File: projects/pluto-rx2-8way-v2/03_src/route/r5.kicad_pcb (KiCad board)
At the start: 4 copper layers, 50 x 73 mm, 32 parts

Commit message: the stranded GND pads were never a search problem: a router reserves a barrel window on the pad's OWN layer and on no other
DRC --severity-all --refill-zones --schematic-parity: 0 violations / 0 unconnected
/ 0 parity, and `rebuild_all.sh` now runs END TO END for the first time on this
board (it was DYING at stitch pass heal_islands, which is a stronger statement
than "2 unconnected": the driver could not complete).

WHAT THE TWO STRANDED PADS ACTUALLY WERE. They are TWO DIFFERENT DEFECTS and
five swept parameters could not have closed either.

R_PD2.2 — MEASURED on the 20:27 board: `via_site_ok` returns TRUE at its own
pad centre, and 144 legal 0.25/0.15 sites exist inside its island. Nothing
about clearance refused it. `pad_rescue` reaches its via through `try_via`,
whose FIRST guard is `stitch.via.spacing` (0.85 mm) measured against EVERY via
already on the board, NET-BLIND — and a SW_V1 escape via sat 0.7440 mm away,
0.106 mm inside a lattice-spacing rule that has nothing to say about a
via-in-pad on a different net. The five swept knobs (island min_bbox, astar
window/attempts, served_within, zone clearance, row pitch) never touched it.

C_SW2.2 — MEASURED: ZERO legal sites out of 608 interior points of its
1.411 x 1.437 mm island, identical at clearance 0.20, 0.14 and 0.13, so not a
clearance question either. Three In2.Cu control verticals ran under one 0.90 mm
pad at x 41.850 / 42.350 / 42.800; a 0.25 barrel needs 0.125 + 0.200 + 0.100 =
0.425 mm from a 0.2 mm centreline, so no site fits between them at any y, and
F.Cu was walled by the 0.400 mm 3V3 trunk and SW_V3. The pad was landlocked.

THE ROOT CAUSE IS ONE SENTENCE AND IT IS GENERAL: a router reserves a barrel
window on the pad's OWN layer automatically — foreign F.Cu centrelines stand
>= 0.45 + 0.20 + 0.10 = 0.75 mm off an 0805 pad centre — and on NO OTHER layer,
because a pad it is not routing is invisible to it there. `waves.exclude: [GND]`
means these pads are never routed at all, so nothing speaks f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
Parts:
- turned C_SW2 to 180 degrees
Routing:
- net 3V3: track 53.7 -> 48.4 mm
- net SW_V3: track 49.7 -> 45.6 mm, vias 8 -> 3
- net SW_V4: track 43.2 -> 45.5 mm
- net LED_STAT_A: track 0.00 -> 1.90 mm, vias 0 -> 2
- net LED_STAT: track 0.00 -> 1.50 mm
- net SW_V2: track 45.4 -> 46.1 mm

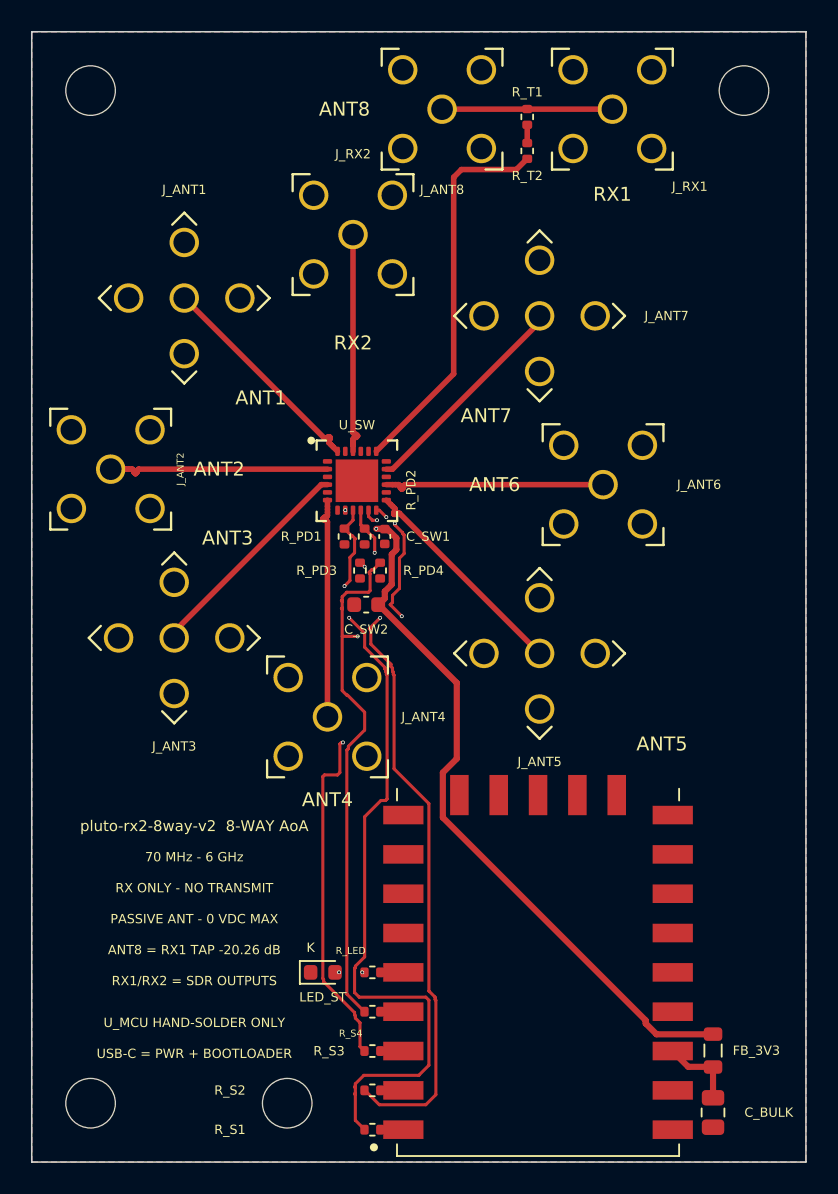
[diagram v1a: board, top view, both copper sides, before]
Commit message: the via fence CLOSED in copper, and the exception that was formed blind is not spent
fence_pitch.py VERDICT: PASS, exit 0. Worst interior along-arm aperture
1.1769 mm against ADR-0004's 1.1910 mm bound, 0 of 22 arm-sides over. It was
17 of 20 at 3.0500. DRC --severity-all --refill-zones --schematic-parity
--exit-code-violations = 0 violations / 0 unconnected / 0 parity.

  17/20 @ 3.0500  inherited (lattice 0.95)
  11/22 @ 3.6000  lattice 0.80 + spacing guard 0.85 -> 0.75
   6/22 @ 3.6000  re-route with the meander length-match pass DELETED
   2/22 @ 1.9769  fence round 1, 14 declared barrels
   1/22 @ 1.9802  fence round 2, 2 barrels
   0/22 @ 1.1769  fence round 3, 1 barrel                       PASS

"OCCUPIED" IS NOT "UNSTITCHABLE". fence_apertures.py names the object NEAREST
an empty LATTICE site — a centre-to-centre distance to a pad centre or a track
MIDPOINT. Read as a verdict it says the SMA-ring and star-hub classes cannot
close. New instrument 03_src/fence_sites.py sweeps the CONTINUUM inside each
aperture's flank band at 0.05 mm and asks the stitcher's OWN via_site_ok
whether a barrel can stand there. Every aperture had legal ground in it. The
SMA `avoid` rings were never the obstruction — their barrels sit OUTSIDE the
ring at 1.36-2.46 mm offset; what could not step aside was the lattice.

THE PITCH ALONE MADE IT WORSE. 0.80 written in by itself emitted 1668 grid
vias where the coarser 0.95 lattice emitted 2208: `stitch.via.spacing` is
try_via's first guard, net-blind, and at 0.85 it sat 0.05 mm ABOVE the new
pitch, so every site refused its neighbour. Green the whole time.

THREE OF MY OWN ESTIMATOR'S ANSWERS WERE WRONG FIRST, ALL TOWARDS INVENTING A
RESIDUAL — the direction that buys an unneeded exception: unsorted marks from
re-projected sites; a greedy walk publishing its give-up point as a physical
limit (ANT5 2.6123 when the floor was 1.3500); and a greedy separated subset
read as a minimax (RX1_MAIN 1.4500 when two sites cover it at 1.0000).
Repl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
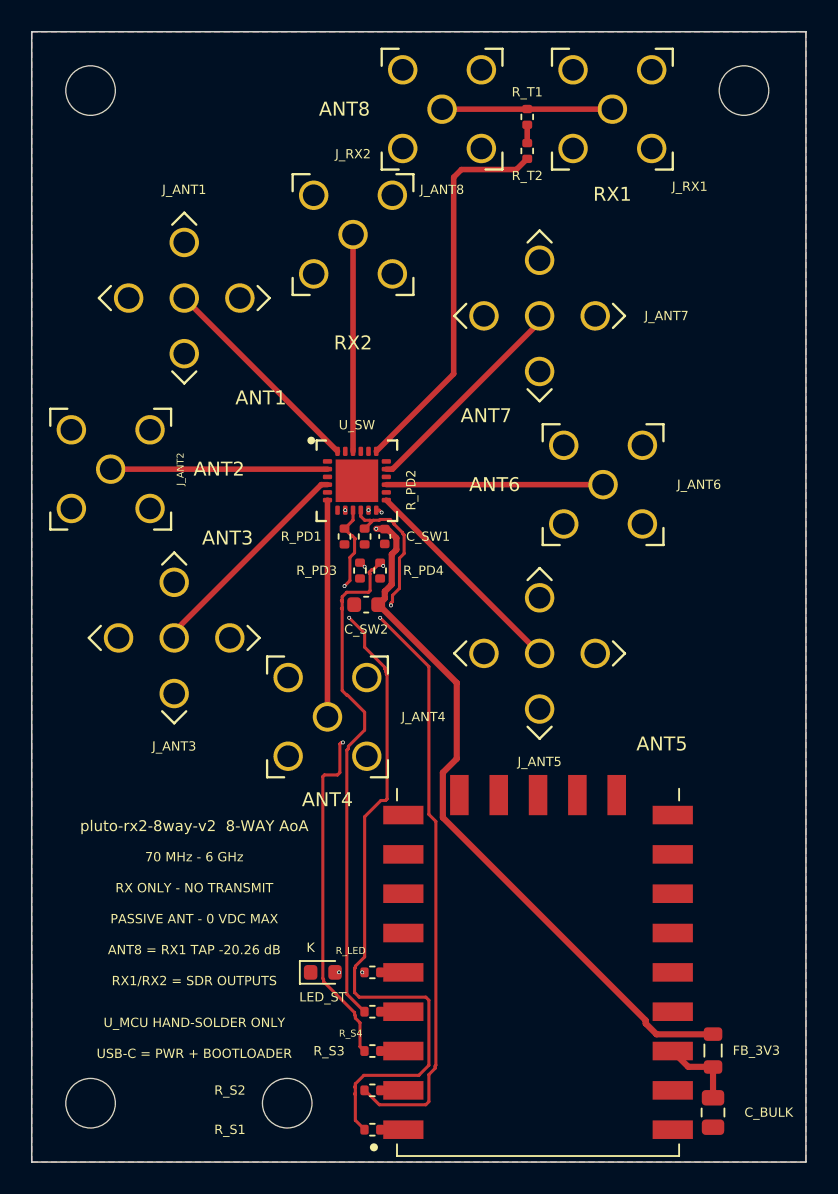
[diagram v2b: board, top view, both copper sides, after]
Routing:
- net SW_V4: track 45.5 -> 37.9 mm, vias 4 -> 2
- net SW_V3: track 45.6 -> 40.7 mm
- net SW_V2: track 46.1 -> 48.1 mm
